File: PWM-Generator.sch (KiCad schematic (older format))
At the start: 2 parts

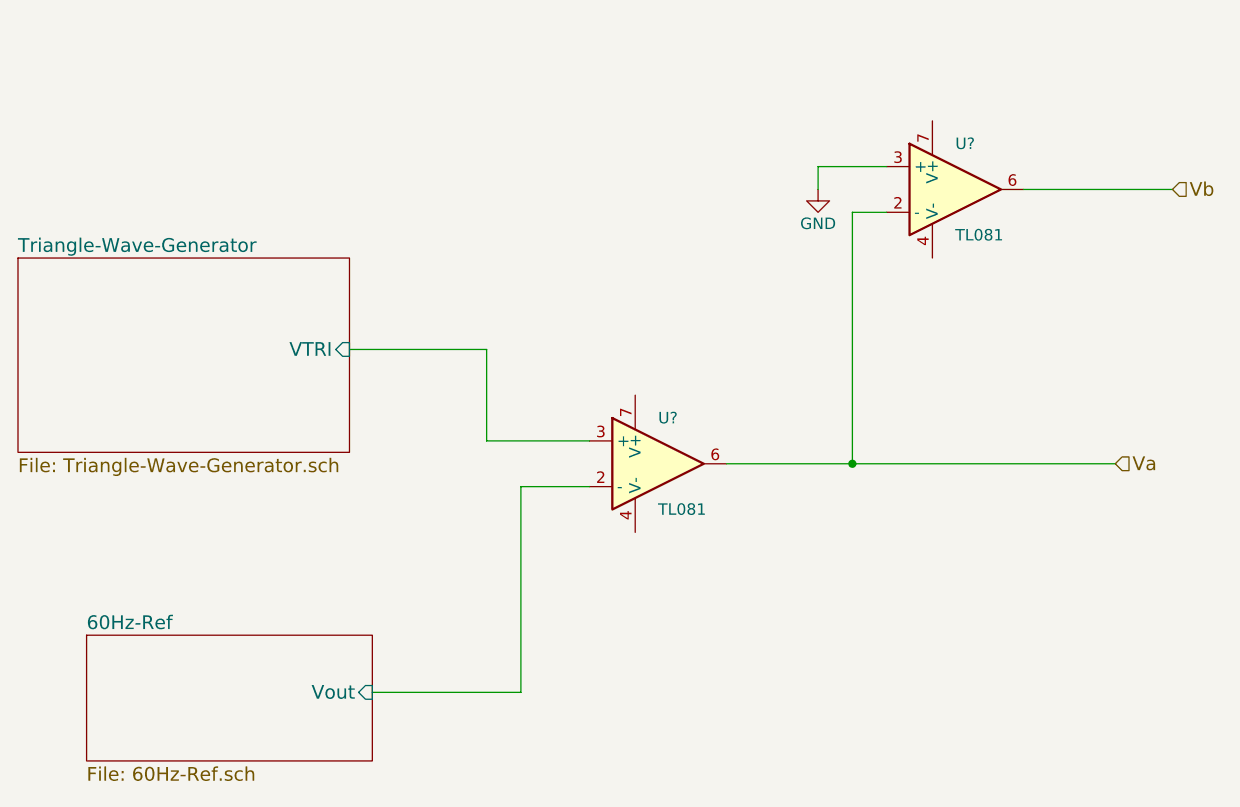
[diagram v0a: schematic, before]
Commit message: Added the basic Schematic
PWM generators work for given reference design values. (LAB Tested)
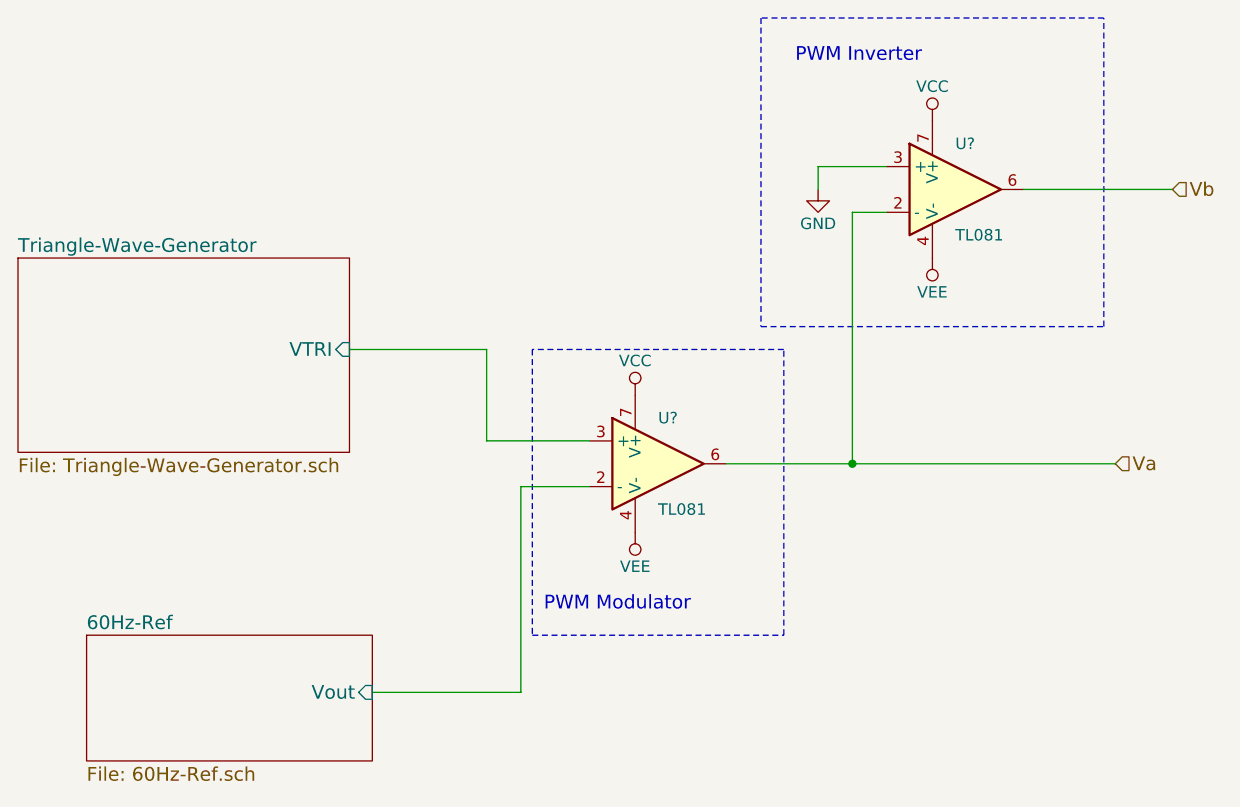
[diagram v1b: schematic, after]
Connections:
- net VEE: now reaches U?.4 (V-)
- net VEE: now also U?.4 (V-)
- net VCC: now reaches U?.7 (V+)
- net VCC: now also U?.7 (V+)
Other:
- note added: "PWM Inverter"
- note added: "PWM Modulator"
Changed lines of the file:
@@
 LIBS:contrib
 LIBS:valves
-LIBS:Buck Supply-cache
 LIBS:H-Bridge PWM Switching Circuit-cache
 EELAYER 25 0
@@
 Wire Wire Line
 	4650 2650 4050 2650
+Wire Notes Line
+	4850 2650 4850 3900
+Wire Notes Line
+	4850 3900 5950 3900
+Wire Notes Line
+	5950 3900 5950 2650
+Wire Notes Line
+	5950 2650 4850 2650
+Text Notes 4900 3800 0    60   ~ 0
+PWM Modulator
+Wire Notes Line
+	5850 1200 5850 2550
+Wire Notes Line
+	5850 2550 7350 2550
+Wire Notes Line
+	7350 2550 7350 1200
+Wire Notes Line
+	7350 1200 5850 1200
+Text Notes 6000 1400 0    60   ~ 0
+PWM Inverter
+$Comp
+L VEE #PWR?
+U 1 1 58EFE0BA
+P 5300 3450
+F 0 "#PWR?" H 5300 3300 50  0001 C CNN
+F 1 "VEE" H 5300 3600 50  0000 C CNN
+F 2 "" H 5300 3450 50  0000 C CNN
+F 3 "" H 5300 3450 50  0000 C CNN
+	1    5300 3450
+	-1   0    0    1
+$EndComp
+$Comp
+L VEE #PWR?
+U 1 1 58EFE0E6
+P 6600 2250
+F 0 "#PWR?" H 6600 2100 50  0001 C CNN
+F 1 "VEE" H 6600 2400 50  0000 C CNN
+F 2 "" H 6600 2250 50  0000 C CNN
+F 3 "" H 6600 2250 50  0000 C CNN
+	1    6600 2250
+	-1   0    0    1
+$EndComp
+$Comp
+L VCC #PWR?
+U 1 1 58EFE112
+P 6600 1650
+F 0 "#PWR?" H 6600 1500 50  0001 C CNN
+F 1 "VCC" H 6600 1800 50  0000 C CNN
+F 2 "" H 6600 1650 50  0000 C CNN
+F 3 "" H 6600 1650 50  0000 C CNN
+	1    6600 1650
+	1    0    0    -1
+$EndComp
+$Comp
+L VCC #PWR?
+U 1 1 58EFE13E
+P 5300 2850
+F 0 "#PWR?" H 5300 2700 50  0001 C CNN
+F 1 "VCC" H 5300 3000 50  0000 C CNN
+F 2 "" H 5300 2850 50  0000 C CNN
+F 3 "" H 5300 2850 50  0000 C CNN
+	1    5300 2850
+	1    0    0    -1
+$EndComp
 $EndSCHEMATC
